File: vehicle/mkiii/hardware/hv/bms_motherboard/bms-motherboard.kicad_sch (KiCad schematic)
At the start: 23 parts, among them J2 EHT-110-01-F-D, J3 EHT-110-01-F-D, J4 CONN_pcie_x1, J5 CONN_pcie_x4, J6 EHT-110-01-F-D

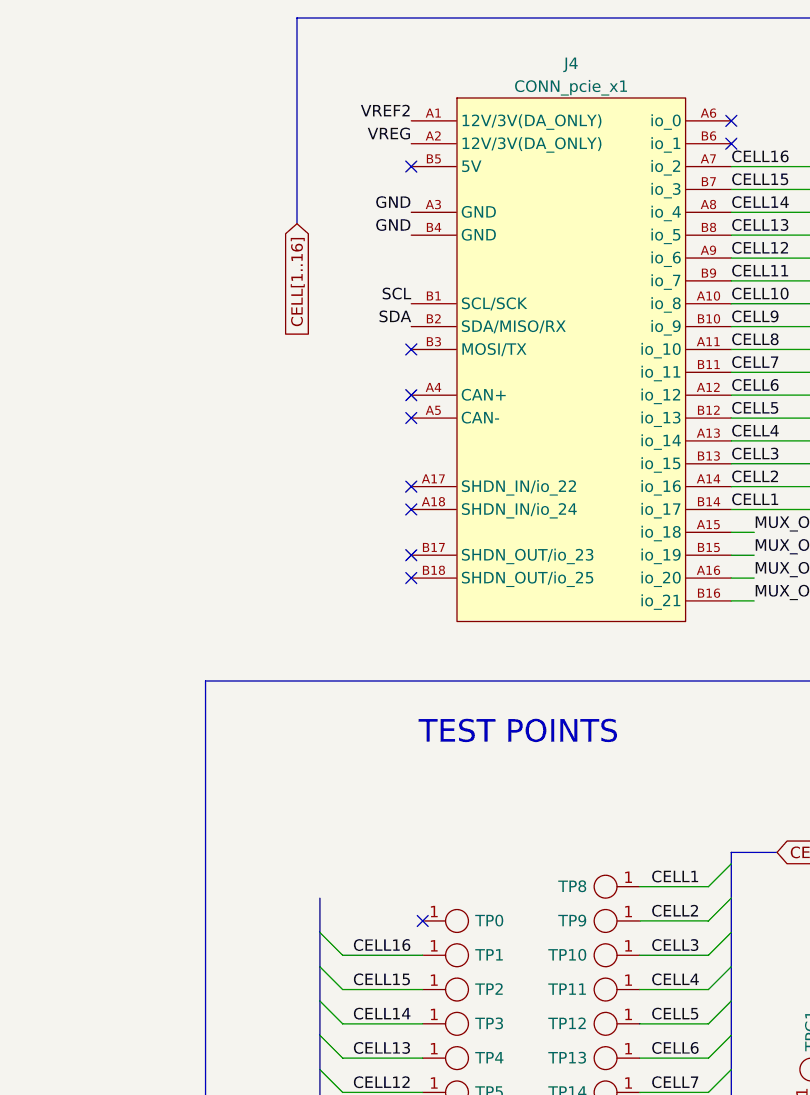
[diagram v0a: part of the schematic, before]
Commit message: Restructured various things; corrected Schematics and PCB layout (Added Cell 16 to 5V pin for CSC PCIe, removed TP0, other changes); added production files.
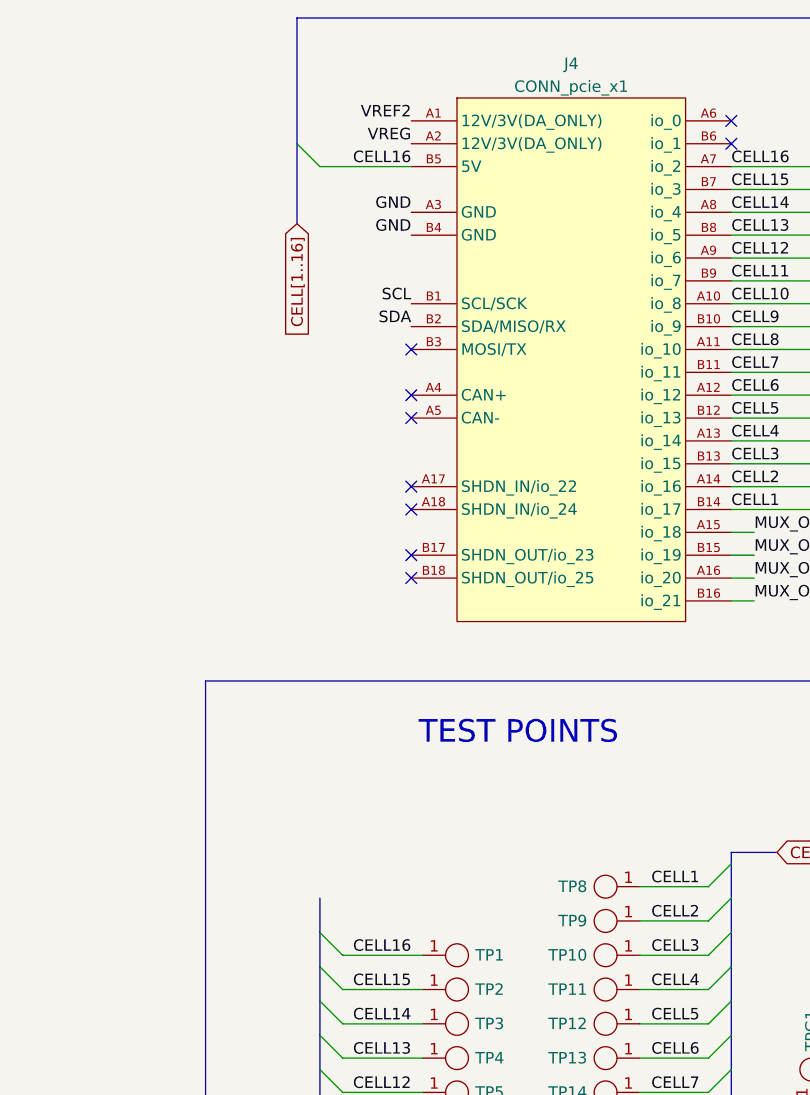
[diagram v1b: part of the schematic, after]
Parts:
- removed TP0: TP_SMD, OEM:Test_Point_SMD, symbol OEM:TP_SMD
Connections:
- net CELL16: now also J4.B5 (5V)
- no-connect marks 27 -> 25
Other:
- title: (none) -> BMS Motherboard
